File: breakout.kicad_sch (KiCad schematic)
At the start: 5 parts, among them U1 STS4X

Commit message: put the projects into one
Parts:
- removed U1: STS4X, STS4X:STS4X, symbol STS4X:STS4X
- added U1: SHT4x, Sensor_Humidity:Sensirion_DFN-4_1.5x1.5mm_P0.8mm_SHT4x_NoCentralPad, symbol Sensor_Humidity:SHT4x
- added U2: STS4X, STS4X:STS4X, symbol STS4X:STS4X
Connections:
- net GND: now also U1.3 (VDD), U2.3 (VDD)
- net VSS: now also U1.4 (VSS), U2.4 (VSS)
- net at H1.1: now also U1.2 (SCL), U2.2 (SCL)
- net at H2.1: now also U1.1 (SDA), U2.1 (SDA)
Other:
- moved on the sheet: H1, H2, H3, H4

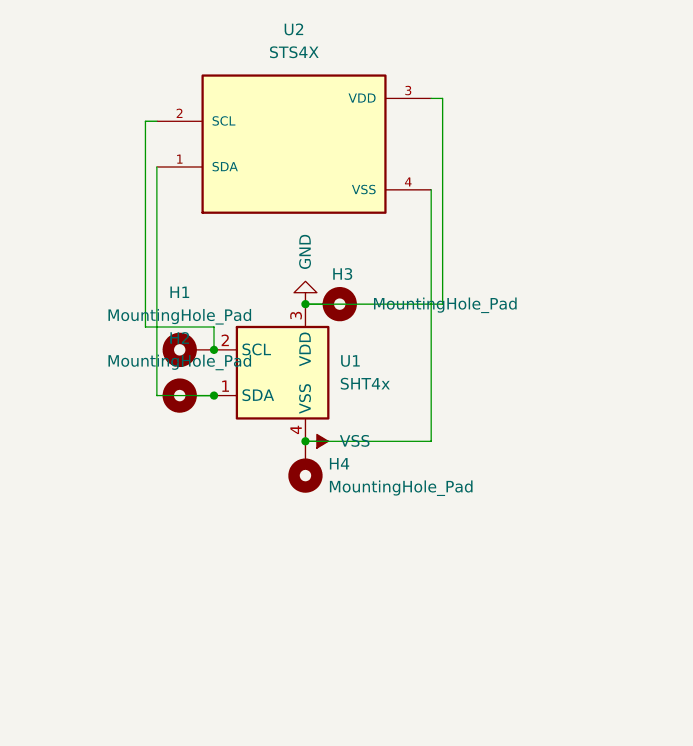
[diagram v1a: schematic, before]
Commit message: make the breakouts separate but in one pcb
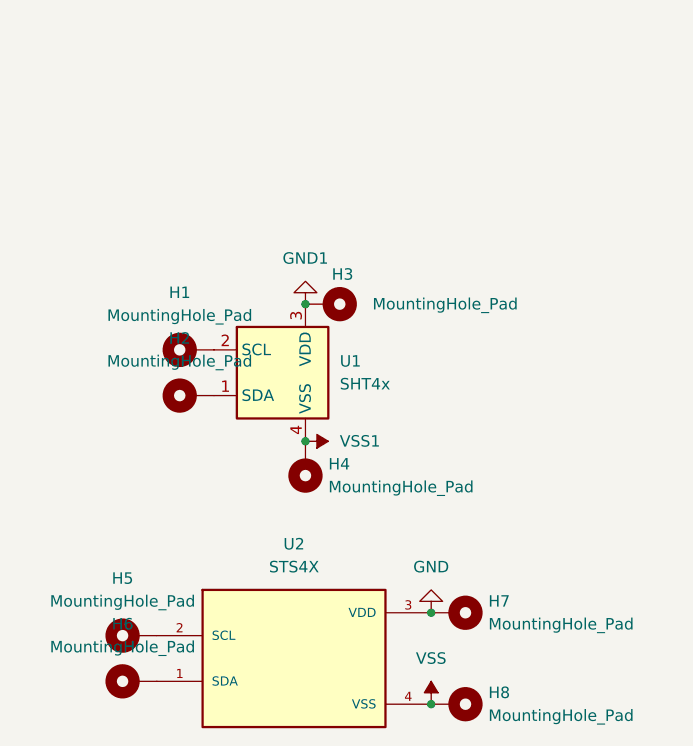
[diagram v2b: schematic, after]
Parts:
- added H5, H6, H7, H8: MountingHole_Pad, MountingHole:MountingHole_2.2mm_M2_DIN965_Pad, symbol Mechanical:MountingHole_Pad
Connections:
- net GND: now also H7.1; no longer H3.1, U1.3 (VDD)
- net VSS: now also H8.1; no longer H4.1, U1.4 (VSS)
- net at H2.1, U1.1 (SDA): no longer U2.1 (SDA)
- net at H1.1, U1.2 (SCL): no longer U2.2 (SCL)
- new net: H5.1, U2.2 (SCL)
- new net: H6.1, U2.1 (SDA)
- new net GND1: H3.1, U1.3 (VDD)
- new net VSS1: H4.1, U1.4 (VSS)
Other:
- moved on the sheet: U2
